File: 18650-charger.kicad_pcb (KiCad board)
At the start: 4 copper layers, 102.6 x 44.8 mm, 36 parts, among them J1 USB4505-03-0-A_REVA, U1 LTC4121IUDTRPBF, U2 LTC4121IUDTRPBF

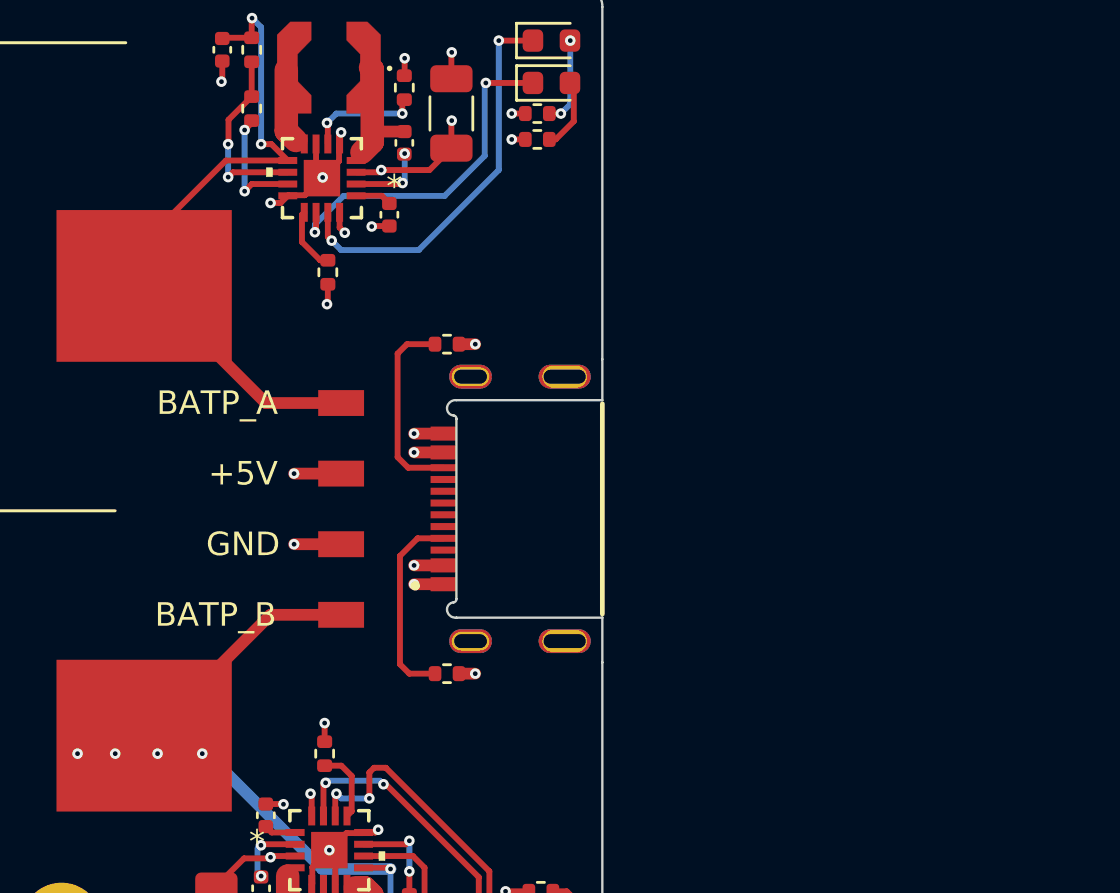
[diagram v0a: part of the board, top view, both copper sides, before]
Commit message: [WIP] Schematic updated with reverse blocking FETs
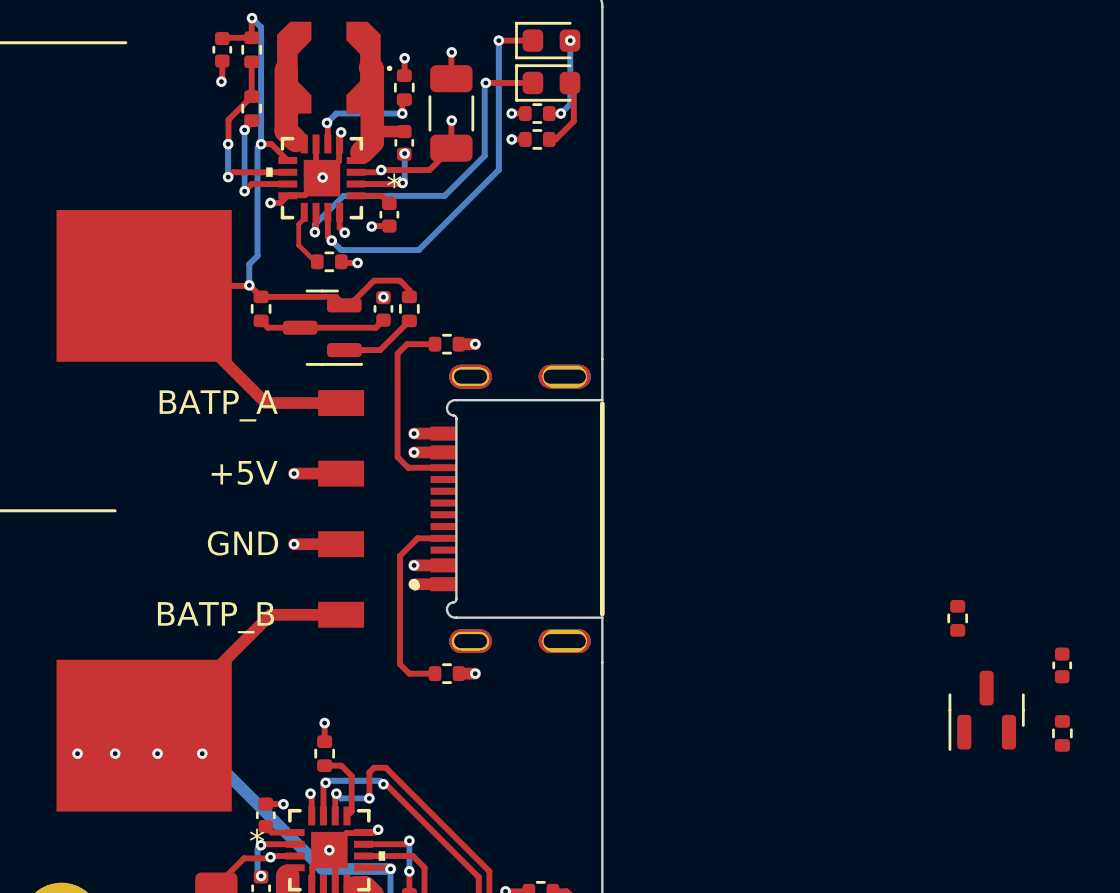
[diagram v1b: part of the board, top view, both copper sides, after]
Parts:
- added C3: 4.7uF, Capacitor_SMD:C_0402_1005Metric, F.Cu at (202.3, 106.5)
- added C8: 4.7uF, Capacitor_SMD:C_0402_1005Metric, F.Cu at (231.1, 121.7)
- added Q1: SI2343DS, Package_TO_SOT_SMD:SOT-23, F.Cu at (199.7, 107.3)
- added Q2: SI2343DS, Package_TO_SOT_SMD:SOT-23, F.Cu at (227.9, 123.5)
- added R15: 470K, Resistor_SMD:R_0402_1005Metric, F.Cu at (226.7, 119.7)
- added R16: 50K, Resistor_SMD:R_0402_1005Metric, F.Cu at (231.2, 124.5)
- added R7: 470K, Resistor_SMD:R_0402_1005Metric, F.Cu at (197.1, 106.5)
- added R8: 50K, Resistor_SMD:R_0402_1005Metric, F.Cu at (203.4, 106.5)
- L3, L6: value 47nH -> 47uH
- moved R3 0.45 mm to (200.0, 104.5), turned to 180 degrees
- renumbered C7 to C10, C3 to C5, C5 to C6, C6 to C7, C8 to C9, R6 to R10, R9 to R11, R10 to R12, R11 to R17, R12 to R18, R7 to R5, R8 to R6, R5 to R9
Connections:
- U1 pad 9: /Charger A/BAT_P -> Net-(C3-Pad1)
- U2 pad 9: /Charger B/BAT_P -> Net-(C8-Pad1)
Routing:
- net /Charger A/BAT_P: track 28.9 -> 38.2 mm, vias 2 -> 3
- net Net-(C3-Pad1): track 0.00 -> 5.45 mm
- net Net-(L2-Pad1): track 14.7 -> 18.0 mm
- net GND: track 27.2 -> 27.1 mm, vias 28 -> 29
